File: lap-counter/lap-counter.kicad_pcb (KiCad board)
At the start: 2 copper layers, 48.3 x 78.7 mm, 23 parts, among them U1 TLP3543

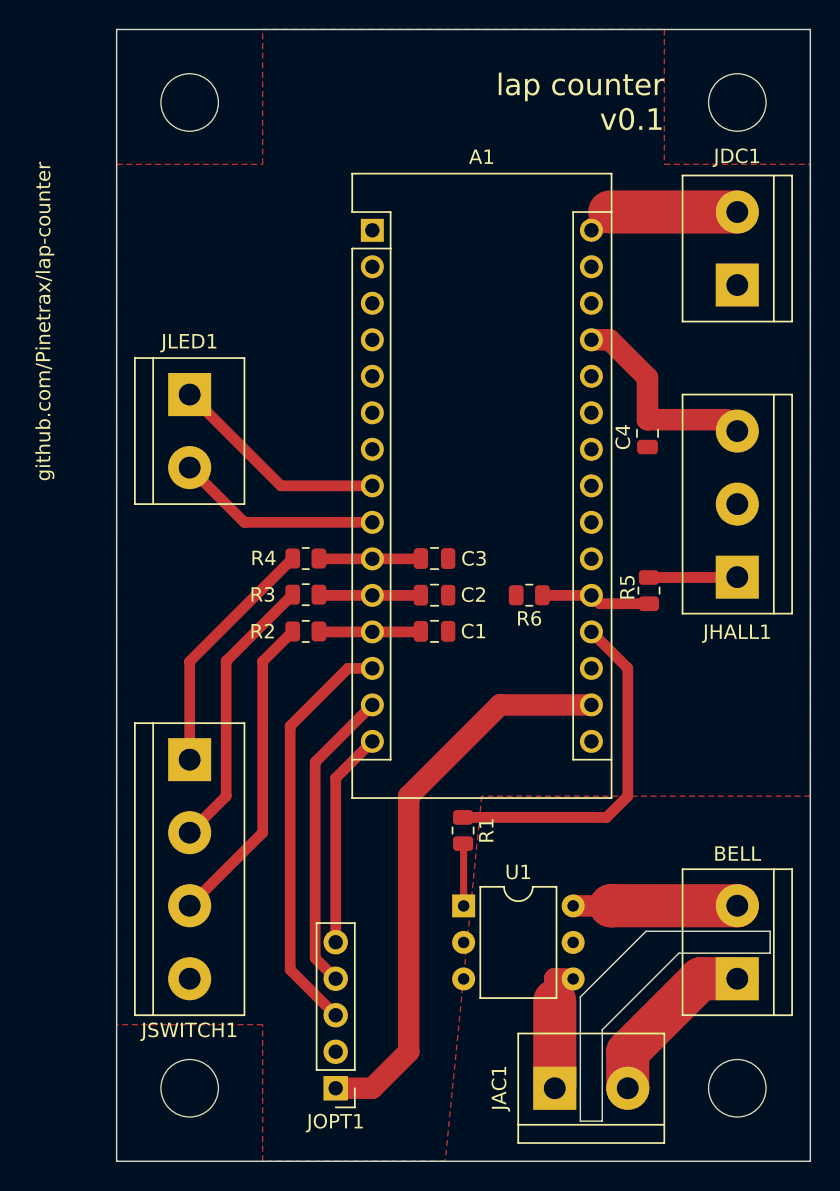
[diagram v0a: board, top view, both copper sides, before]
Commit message: Optimize trace layout and ground plane
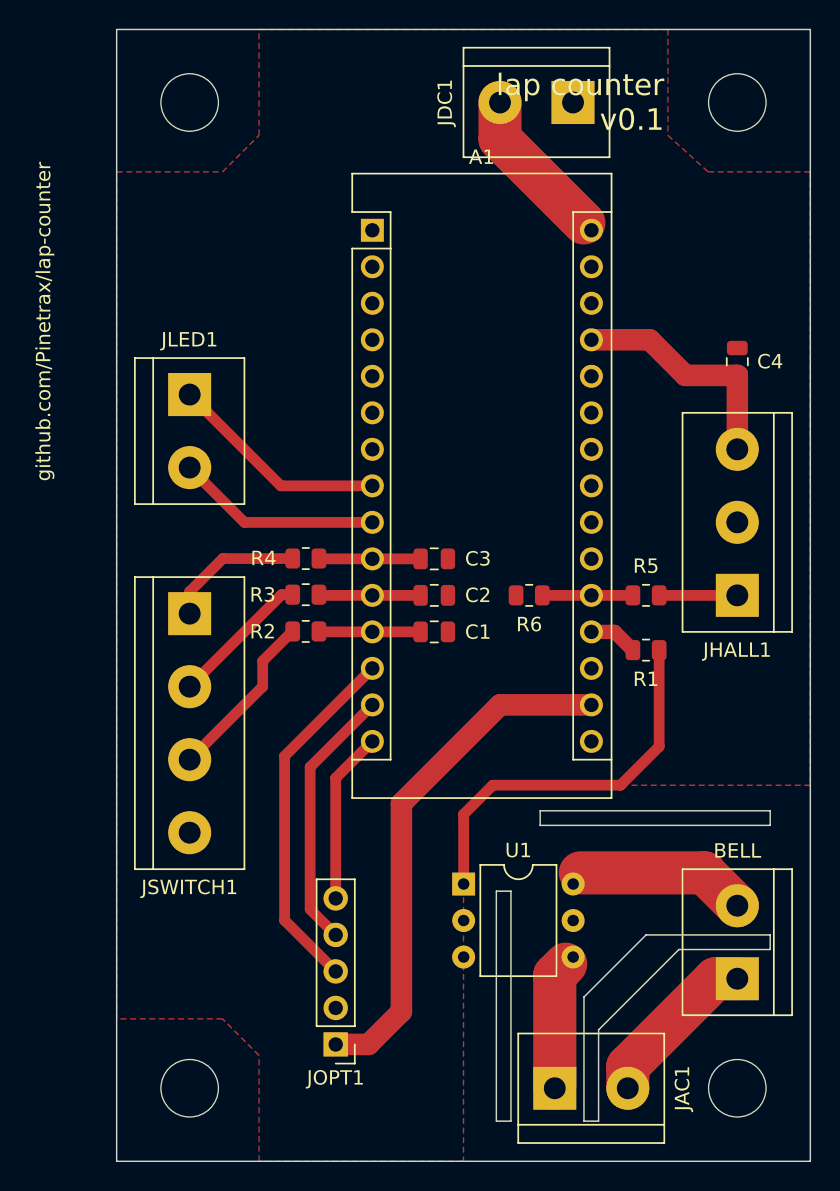
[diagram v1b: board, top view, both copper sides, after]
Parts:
- moved R1 17.9 mm to (156.2, 68.6), turned to 0 degrees
- moved JDC1 17.1 mm to (151.1, 30.5), turned to 180 degrees
- moved JSWITCH1 10.2 mm to (124.5, 66.0)
- moved C4 7.99 mm to (162.6, 48.5), turned to -90 degrees
- moved JOPT1 3.05 mm to (134.6, 96.0)
- moved U1 1.52 mm to (143.5, 84.9)
- moved JHALL1 1.27 mm to (162.6, 64.8)
- moved R5 0.39 mm to (156.2, 64.8), turned to 180 degrees
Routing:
- net Net-(R1-Pad2): track 4.35 -> 27.1 mm
- net Net-(R1-Pad1): track 24.5 -> 3.41 mm
- net Net-(JSWITCH1-Pad3): track 22.0 -> 11.9 mm
- net Net-(R3-Pad2): track 19.5 -> 9.82 mm
- net Net-(R4-Pad2): track 17.0 -> 9.65 mm
- net Net-(JOPT1-Pad3): track 28.8 -> 25.1 mm
- net +3.3V: track 39.3 -> 36.1 mm
- net Net-(A1-Pad15): track 15.0 -> 12.0 mm
- net Net-(JOPT1-Pad4): track 21.3 -> 18.5 mm
- net +5V: track 14.5 -> 16.3 mm
- net Net-(U1-Pad6): track 11.4 -> 12.9 mm
- net Net-(R5-Pad2): track 7.66 -> 6.30 mm
- net +12V: track 10.7 -> 11.5 mm
- net Net-(U1-Pad4): track 8.91 -> 9.67 mm
- net Net-(R5-Pad1): track 6.16 -> 5.44 mm
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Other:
- outline, holes or cut-outs redrawn

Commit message: Raise version to v0.2
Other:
- board text added: "lap counter v0.2"
- board text removed: "lap counter v0.1"
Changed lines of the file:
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@@
   (gr_line (start 164.846 89.408) (end 158.496 89.408) (layer "Edge.Cuts") (width 0.1))
   (gr_line (start 156.21 88.392) (end 164.846 88.392) (layer "Edge.Cuts") (width 0.1))
-  (gr_text "lap counter\nv0.1" (at 157.48 30.48) (layer "F.SilkS")
-    (effects (font (size 1.5 1.5) (thickness 0.25)) (justify right))
+  (gr_text "lap counter\nv0.2" (at 120.142 38.1) (layer "F.SilkS")
+    (effects (font (size 1.5 1.5) (thickness 0.25)) (justify left))
   )
   (gr_text "github.com/Pinetrax/lap-counter" (at 114.3 45.72 90) (layer "F.SilkS")

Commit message: Review and raise version to v1.0
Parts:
- JAC1, JBELL1, JDC1, JLED1: footprint TerminalBlock:TerminalBlock_bornier-2_P5.08mm -> Connector_Molex:Molex_Micro-Fit_3.0_43650-0215_1x02_P3.00mm_Vertical
- JHALL1: footprint TerminalBlock:TerminalBlock_bornier-3_P5.08mm -> Connector_Molex:Molex_Micro-Fit_3.0_43650-0315_1x03_P3.00mm_Vertical
- JOPT1: footprint Connector_PinHeader_2.54mm:PinHeader_1x05_P2.54mm_Vertical -> Connector_Molex:Molex_Micro-Fit_3.0_43650-0515_1x05_P3.00mm_Vertical
- JSWITCH1: footprint TerminalBlock:TerminalBlock_bornier-4_P5.08mm -> Connector_Molex:Molex_Micro-Fit_3.0_43650-0415_1x04_P3.00mm_Vertical
- moved C4 5.04 mm to (159.3, 52.3), turned to 180 degrees
- moved JDC1 3.19 mm to (148.1, 29.6)
- moved JOPT1 3.03 mm to (134.0, 99.0), turned to 90 degrees
- moved JBELL1 1.35 mm to (163.4, 90.4)
- moved JAC1 1.16 mm to (150.6, 99.9)
- moved R3 1.07 mm to (133.6, 64.8)
- moved R2 1.07 mm to (133.6, 67.3)
- moved R4 1.07 mm to (133.6, 62.2)
- moved JHALL1 0.85 mm to (163.4, 64.8)
- moved JLED1 0.85 mm to (123.6, 50.8)
- moved JSWITCH1 0.85 mm to (123.6, 66.0)
- moved R5 0.25 mm to (156.0, 64.8)
- renumbered A1 to AR1
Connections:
- JDC1 pad 1: GND -> +12V
- JDC1 pad 2: +12V -> GND
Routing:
- net +5V: track 16.3 -> 20.5 mm
- net Net-(JAC1-Pad2): track 11.7 -> 15.7 mm
- net +3.3V: track 36.1 -> 40.0 mm
- net Net-(AR1-Pad13): track 25.1 -> 28.9 mm
- net Net-(AR1-Pad14): track 18.5 -> 21.9 mm
- net Net-(AR1-Pad9): track 14.3 -> 16.0 mm
- net Net-(AR1-Pad15): track 12.0 -> 13.4 mm
- net Net-(JHALL1-Pad1): track 5.44 -> 6.55 mm
- net Net-(AR1-Pad11): track 7.10 -> 6.01 mm
- net Net-(AR1-Pad12): track 7.09 -> 6.01 mm
- net Net-(AR1-Pad10): track 7.09 -> 6.01 mm
- net Net-(JSWITCH1-Pad2): track 9.82 -> 10.9 mm
- net Net-(JSWITCH1-Pad1): track 9.65 -> 10.7 mm
- net Net-(JSWITCH1-Pad3): track 11.9 -> 11.0 mm
- net Net-(AR1-Pad8): track 15.3 -> 16.2 mm
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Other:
- outline, holes or cut-outs redrawn
- board text added: "+3.3V"
- board text added: "+5V"
- board text added: "A1"
- board text added: "AC"
- board text added: "D10"
- board text added: "D11"
- board text added: "D12"
- board text added: "D13"
- board text added: "D14"
- board text added: "D15"
- board text added: "D8"
- board text added: "D9"
- board text added: "GND"
- board text added: "V_IN"
- board text added: "lap counter v1.0"
- board text removed: "BELL"
- board text removed: "lap counter v0.2"

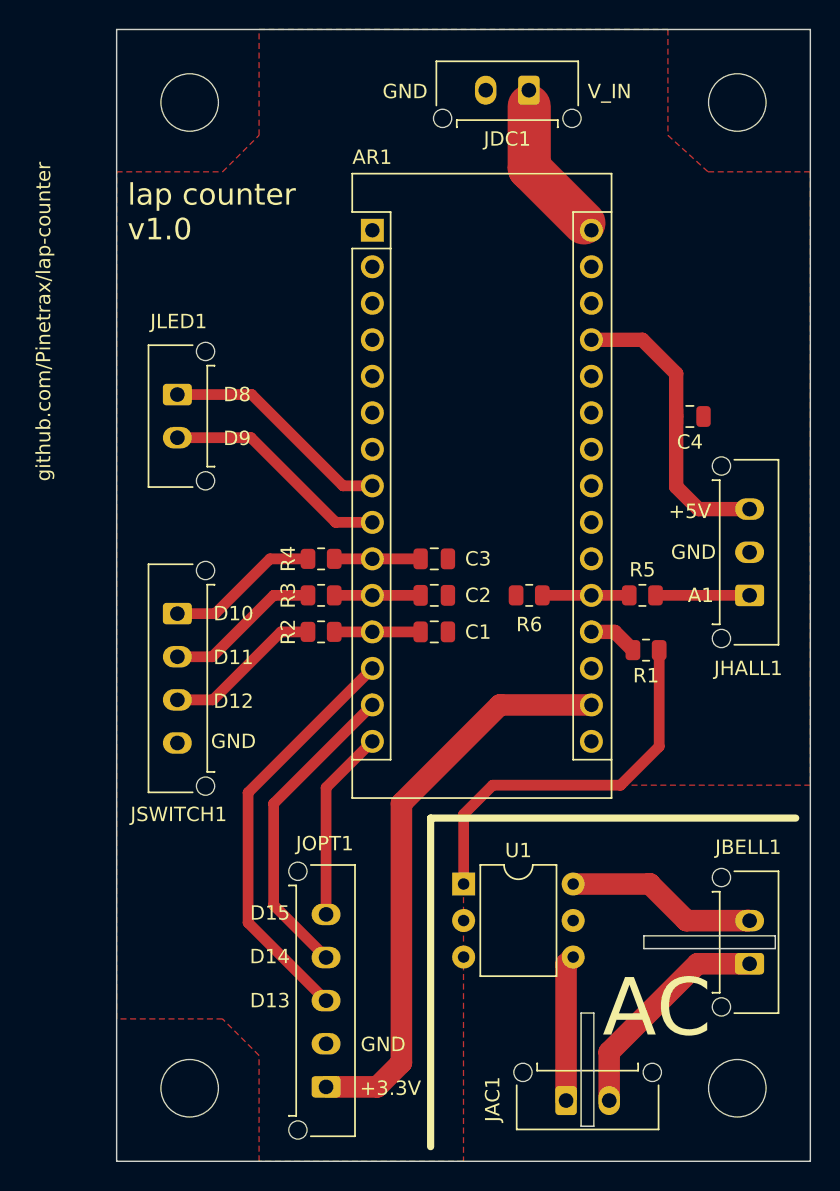
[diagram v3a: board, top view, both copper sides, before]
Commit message: Raise version to 1.1 with minor improvements, use gitignore
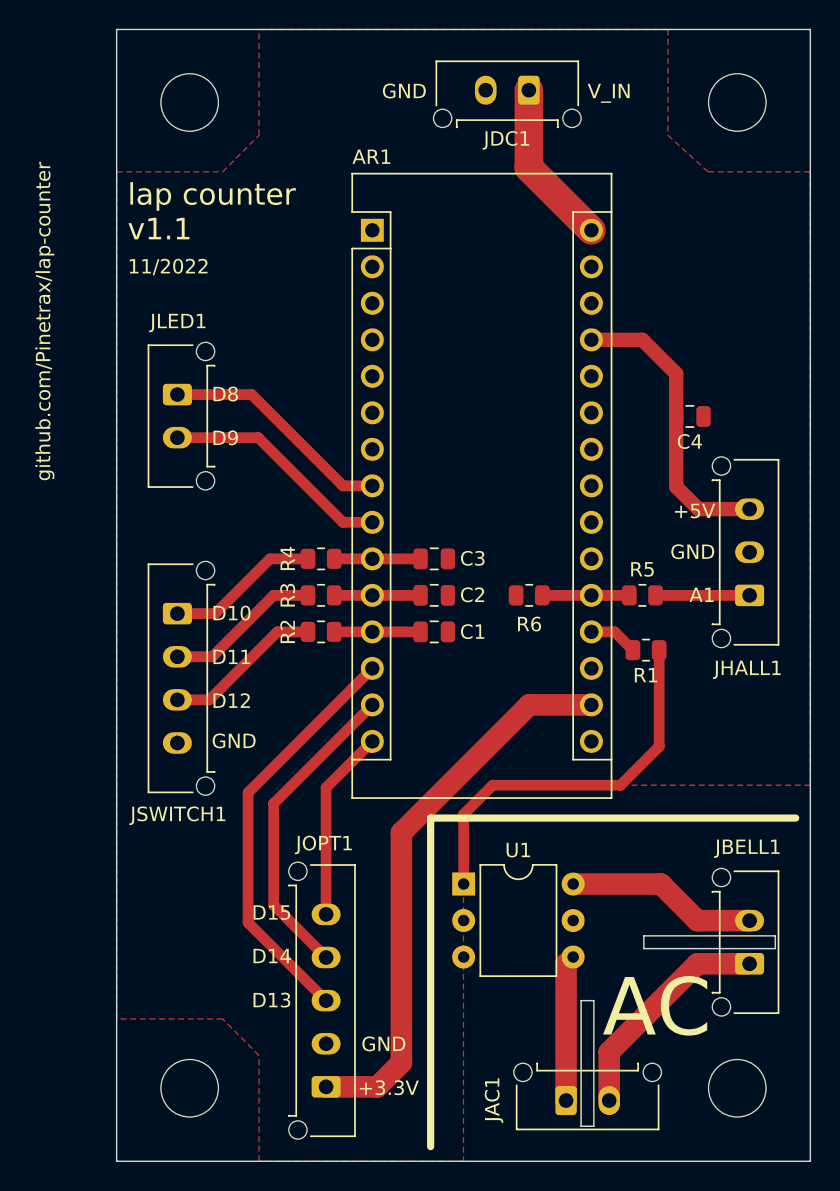
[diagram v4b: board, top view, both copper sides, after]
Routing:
- net +3.3V: track 40.0 -> 38.8 mm
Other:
- outline, holes or cut-outs redrawn
- board text added: "11/2022"
- board text added: "lap counter v1.1"
- board text removed: "lap counter v1.0"
